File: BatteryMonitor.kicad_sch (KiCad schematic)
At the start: 26 parts, among them J5 Fuel Gauge Programming Header, U5 MAX17205

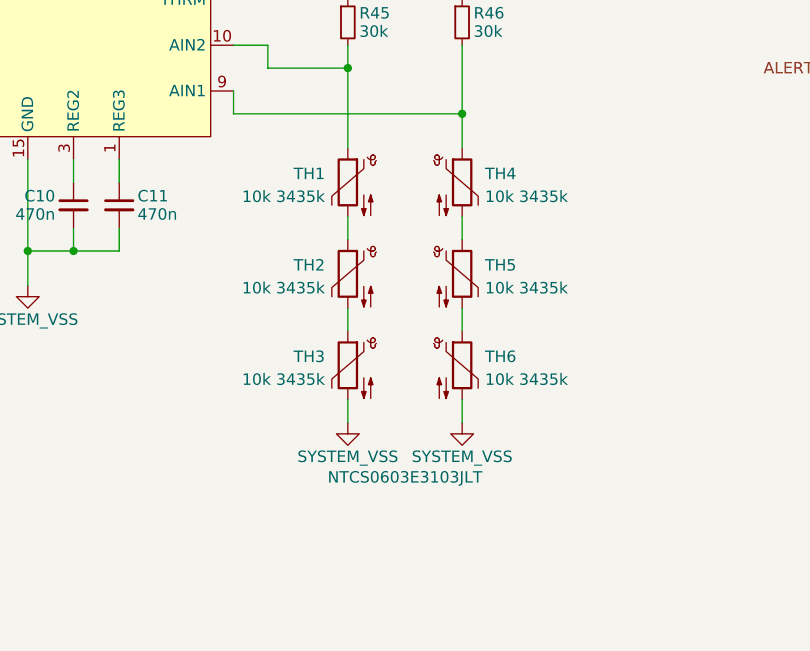
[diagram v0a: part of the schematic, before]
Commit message: Updates board to 2s2p configuration.
Removes 2 cells from Battery, 2 thermistors from Battery Monitor, and 2 heater from BatteryHeater an BatteryHeater1
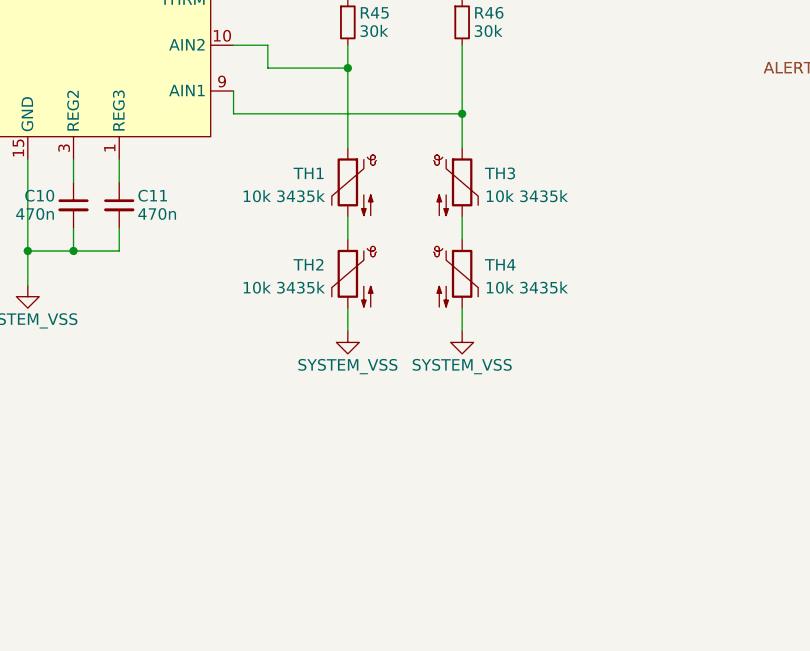
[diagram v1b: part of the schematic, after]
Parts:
- removed TH1, TH6: 10k 3435k, Capacitor_SMD:C_0603_1608Metric, symbol Device:Thermistor_NTC
- renumbered TH2 to TH1, TH3 to TH2, TH4 to TH3, TH5 to TH4
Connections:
- net SYSTEM_VSS: now also TH4.2
- net at TH1.1: now also R45.2, U5.10 (AIN2)
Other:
- moved on the sheet: TH1, TH2
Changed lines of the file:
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@@
 	(wire
 		(pts
-			(xy 132.08 143.51) (xy 132.08 146.05)
+			(xy 132.08 133.35) (xy 132.08 135.89)
 		)
 		(stroke
@@
 	(wire
 		(pts
-			(xy 132.08 133.35) (xy 132.08 135.89)
+			(xy 132.08 123.19) (xy 132.08 125.73)
 		)
 		(stroke
@@
 	(wire
 		(pts
-			(xy 144.78 143.51) (xy 144.78 146.05)
-		)
-		(stroke
-			(width 0)
-			(type default)
-		)
-	)
-	(wire
-		(pts
 			(xy 96.52 127) (xy 96.52 116.84)
 		)
@@
 	(wire
 		(pts
-			(xy 132.08 123.19) (xy 132.08 125.73)
-		)
-		(stroke
-			(width 0)
-			(type default)
-		)
-	)
-	(wire
-		(pts
 			(xy 185.42 106.68) (xy 191.77 106.68)
 		)
@@
 		(dnp no)
 		(fields_autoplaced yes)
-		(property "Reference" "TH5"
+		(property "Reference" "TH4"
 			(at 147.32 128.5874 0)
 			(effects
@@
 			(project "BatteryBoard"
 				(path "/b6fd875d-6e05-4440-9a05-0f0aa046a0ef/ad142cc2-d77f-4a6c-99c2-d9e17f4c27ae"
-					(reference "TH5")
+					(reference "TH4")
 					(unit 1)
 				)
@@
 	)
 	(symbol
-		(lib_id "Device:Thermistor_NTC")
-		(at 144.78 139.7 0)
-		(unit 1)
-		(exclude_from_sim no)
-		(in_bom yes)
-		(on_board yes)
-		(dnp no)
-		(fields_autoplaced yes)
-		(property "Reference" "TH6"
-			(at 147.32 138.7474 0)
-			(effects
-				(font
-					(size 1.27 1.27)
-				)
-				(justify left)
-			)
-		)
-		(property "Value" "10k 3435k"
-			(at 147.32 141.2874 0)
-			(effects
-				(font
-					(size 1.27 1.27)
-				)
-				(justify left)
-			)
-		)
-		(property "Footprint" "Capacitor_SMD:C_0603_1608Metric"
-			(at 144.78 138.43 0)
-			(effects
-				(font
-					(size 1.27 1.27)
-				)
-				(hide yes)
-			)
-		)
-		(property "Datasheet" "~"
-			(at 144.78 138.43 0)
-			(effects
-				(font
-					(size 1.27 1.27)
-				)
-				(hide yes)
-			)
-		)
-		(property "Description" "Temperature dependent resistor, negative temperature coefficient"
-			(at 144.78 139.7 0)
-			(effects
-				(font
-					(size 1.27 1.27)
-				)
-				(hide yes)
-			)
-		)
-		(pin "2"
-		)
-		(pin "1"
-		)
-		(instances
-			(project "BatteryBoard"
-				(path "/b6fd875d-6e05-4440-9a05-0f0aa046a0ef/ad142cc2-d77f-4a6c-99c2-d9e17f4c27ae"
-					(reference "TH6")
-					(unit 1)
-				)
-			)
-		)
-	)
-	(symbol
 		(lib_id "power:GND")
 		(at 67.31 109.22 0)
@@
 	(symbol
 		(lib_id "power:GND")
-		(at 144.78 146.05 0)
+		(at 144.78 135.89 0)
 		(unit 1)
 		(exclude_from_sim no)
@@
 		(dnp no)
 		(property "Reference" "#PWR052"
-			(at 144.78 152.4 0)
+			(at 144.78 142.24 0)
 			(effects
 				(font
@@
 		)
 		(property "Value" "SYSTEM_VSS"
-			(at 144.78 149.86 0)
+			(at 144.78 139.7 0)
 			(effects
 				(font
@@
 		)
 		(property "Footprint" ""
-			(at 144.78 146.05 0)
+			(at 144.78 135.89 0)
 			(effects
 				(font
@@
 		)
 		(property "Datasheet" ""
-			(at 144.78 146.05 0)
+			(at 144.78 135.89 0)
 			(effects
 				(font
@@
 		)
 		(property "Description" "Power symbol creates a global label with name \"GND\" , ground"
-			(at 144.78 146.05 0)
+			(at 144.78 135.89 0)
 			(effects
 				(font
@@
 	(symbol
 		(lib_id "Device:Thermistor_NTC")
-		(at 132.08 129.54 0)
+		(at 132.08 119.38 0)
 		(mirror y)
 		(unit 1)
@@
 		(on_board yes)
 		(dnp no)
-		(property "Reference" "TH2"
-			(at 129.54 128.5874 0)
+		(property "Reference" "TH1"
+			(at 129.54 118.4274 0)
 			(effects
 				(font
@@
 		)
 		(property "Value" "10k 3435k"
-			(at 129.54 131.1274 0)
+			(at 129.54 120.9674 0)
 			(effects
 				(font
@@
 		)
 		(property "Footprint" "Capacitor_SMD:C_0603_1608Metric"
-			(at 132.08 128.27 0)
+			(at 132.08 118.11 0)
 			(effects
 				(font
@@
 		)
 		(property "Datasheet" "~"
-			(at 132.08 128.27 0)
+			(at 132.08 118.11 0)
 			(effects
 				(font
@@
 		)
 		(property "Description" "Temperature dependent resistor, negative temperature coefficient"
-			(at 132.08 129.54 0)
+			(at 132.08 119.38 0)
 			(effects
 				(font
@@
 			(project "BatteryBoard"
 				(path "/b6fd875d-6e05-4440-9a05-0f0aa046a0ef/ad142cc2-d77f-4a6c-99c2-d9e17f4c27ae"
-					(reference "TH2")
+					(reference "TH1")
 					(unit 1)
 				)
@@
 	(symbol
 		(lib_id "Device:Thermistor_NTC")
-		(at 132.08 139.7 0)
+		(at 132.08 129.54 0)
 		(mirror y)
 		(unit 1)
@@
 		(on_board yes)
 		(dnp no)
-		(property "Reference" "TH3"
-			(at 129.54 138.7474 0)
+		(property "Reference" "TH2"
+			(at 129.54 128.5874 0)
 			(effects
 				(font
@@
 		)
 		(property "Value" "10k 3435k"
-			(at 129.54 141.2874 0)
+			(at 129.54 131.1274 0)
 			(effects
 				(font
@@
 		)
 		(property "Footprint" "Capacitor_SMD:C_0603_1608Metric"
-			(at 132.08 138.43 0)
+			(at 132.08 128.27 0)
 			(effects
 				(font
@@
 		)
 		(property "Datasheet" "~"
-			(at 132.08 138.43 0)
+			(at 132.08 128.27 0)
 			(effects
 				(font
@@
 		)
 		(property "Description" "Temperature dependent resistor, negative temperature coefficient"
-			(at 132.08 139.7 0)
+			(at 132.08 129.54 0)
 			(effects
 				(font
@@
 			(project "BatteryBoard"
 				(path "/b6fd875d-6e05-4440-9a05-0f0aa046a0ef/ad142cc2-d77f-4a6c-99c2-d9e17f4c27ae"
-					(reference "TH3")
+					(reference "TH2")
 					(unit 1)
 				)
@@
 	(symbol
 		(lib_id "power:GND")
-		(at 132.08 146.05 0)
+		(at 132.08 135.89 0)
 		(unit 1)
 		(exclude_from_sim no)
@@
 		(dnp no)
 		(property "Reference" "#PWR051"
-			(at 132.08 152.4 0)
+			(at 132.08 142.24 0)
 			(effects
 				(font
@@
 		)
 		(property "Value" "SYSTEM_VSS"
-			(at 132.08 149.86 0)
+			(at 132.08 139.7 0)
 			(effects
 				(font
@@
 		)
 		(property "Footprint" ""
-			(at 132.08 146.05 0)
+			(at 132.08 135.89 0)
 			(effects
 				(font
@@
 		)
 		(property "Datasheet" ""
-			(at 132.08 146.05 0)
+			(at 132.08 135.89 0)
 			(effects
 				(font
@@
 		)
 		(property "Description" "Power symbol creates a global label with name \"GND\" , ground"
-			(at 132.08 146.05 0)
+			(at 132.08 135.89 0)
 			(effects
 				(font
@@
 	)
 	(symbol
-		(lib_id "Device:Thermistor_NTC")
-		(at 132.08 119.38 0)
-		(mirror y)
-		(unit 1)
-		(exclude_from_sim no)
-		(in_bom yes)
-		(on_board yes)
-		(dnp no)
-		(property "Reference" "TH1"
-			(at 129.54 118.4274 0)
-			(effects
-				(font
-					(size 1.27 1.27)
-				)
-				(justify left)
-			)
-		)
-		(property "Value" "10k 3435k"
-			(at 129.54 120.9674 0)
-			(effects
-				(font
-					(size 1.27 1.27)
-				)
-				(justify left)
-			)
-		)
-		(property "Footprint" "Capacitor_SMD:C_0603_1608Metric"
-			(at 132.08 118.11 0)
-			(effects
-				(font
-					(size 1.27 1.27)
-				)
-				(hide yes)
-			)
-		)
-		(property "Datasheet" "~"
-			(at 132.08 118.11 0)
-			(effects
-				(font
-					(size 1.27 1.27)
-				)
-				(hide yes)
-			)
-		)
-		(property "Description" "Temperature dependent resistor, negative temperature coefficient"
-			(at 132.08 119.38 0)
-			(effects
-				(font
-					(size 1.27 1.27)
-				)
-				(hide yes)
-			)
-		)
-		(property "Field5" "NTCS0603E3103JLT"
-			(at 138.43 152.146 0)
-			(effects
-				(font
-					(size 1.27 1.27)
-				)
-			)
-		)
-		(pin "2"
-		)
-		(pin "1"
-		)
-		(instances
-			(project ""
-				(path "/b6fd875d-6e05-4440-9a05-0f0aa046a0ef/ad142cc2-d77f-4a6c-99c2-d9e17f4c27ae"
-					(reference "TH1")
-					(unit 1)
-				)
-			)
-		)
-	)
-	(symbol
 		(lib_id "Device:R_Small")
 		(at 200.66 72.39 90)
@@
 		(dnp no)
 		(fields_autoplaced yes)
-		(property "Reference" "TH4"
+		(property "Reference" "TH3"
 			(at 147.32 118.4274 0)
 			(effects
@@
 			(project "BatteryBoard"
 				(path "/b6fd875d-6e05-4440-9a05-0f0aa046a0ef/ad142cc2-d77f-4a6c-99c2-d9e17f4c27ae"
-					(reference "TH4")
+					(reference "TH3")
 					(unit 1)
 				)
@@
 		)
 		(instances
-			(project "Avionics-BatteryBoard"
+			(project "Avionics-Argus3-BatteryBoard"
 				(path "/b6fd875d-6e05-4440-9a05-0f0aa046a0ef/ad142cc2-d77f-4a6c-99c2-d9e17f4c27ae"
 					(page "5")
